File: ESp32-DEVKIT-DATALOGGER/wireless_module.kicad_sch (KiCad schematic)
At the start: 22 parts, among them J201 Socket_01x02, J202 Conn_01x06_Socket, J203 Conn_01x04_Socket, J204 Conn_01x04_Socket, J205 Micro_SD_Card, Q201 MMBT3904, Q202 MMBT3904, SW201 SW_Omron_B3FS, SW202 SW_Omron_B3FS, U201 ESP32-S3-WROOM-1

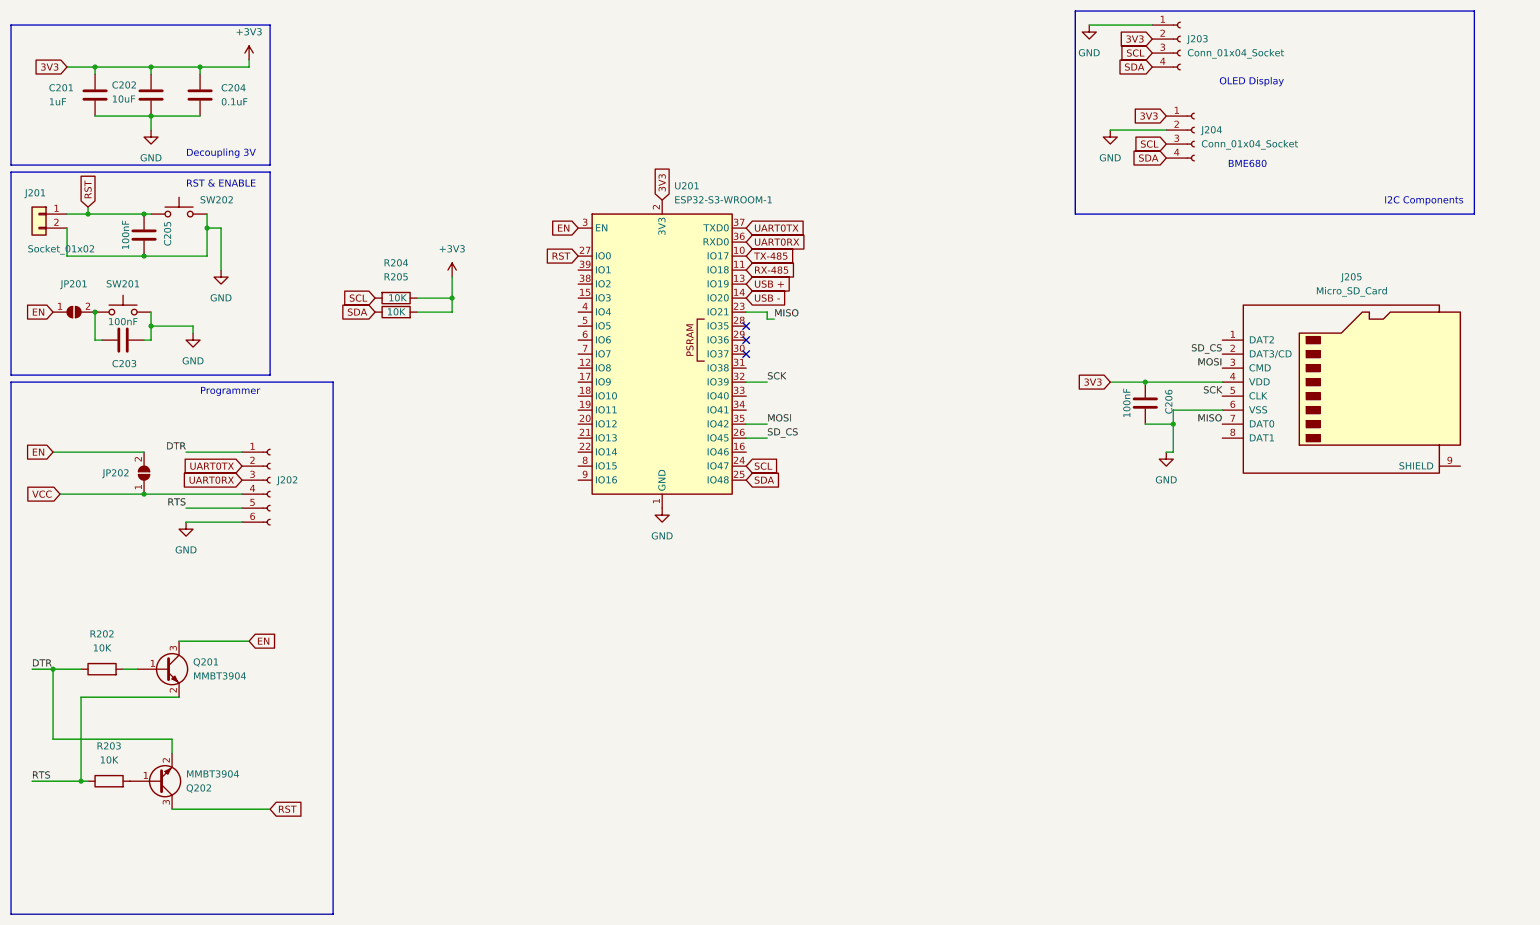
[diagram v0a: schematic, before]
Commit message: Small Changes
Adding I2C components
More RS485
And it is required changing the  Labels for RS485 . for 3 different channels
And Make them ISO Pins
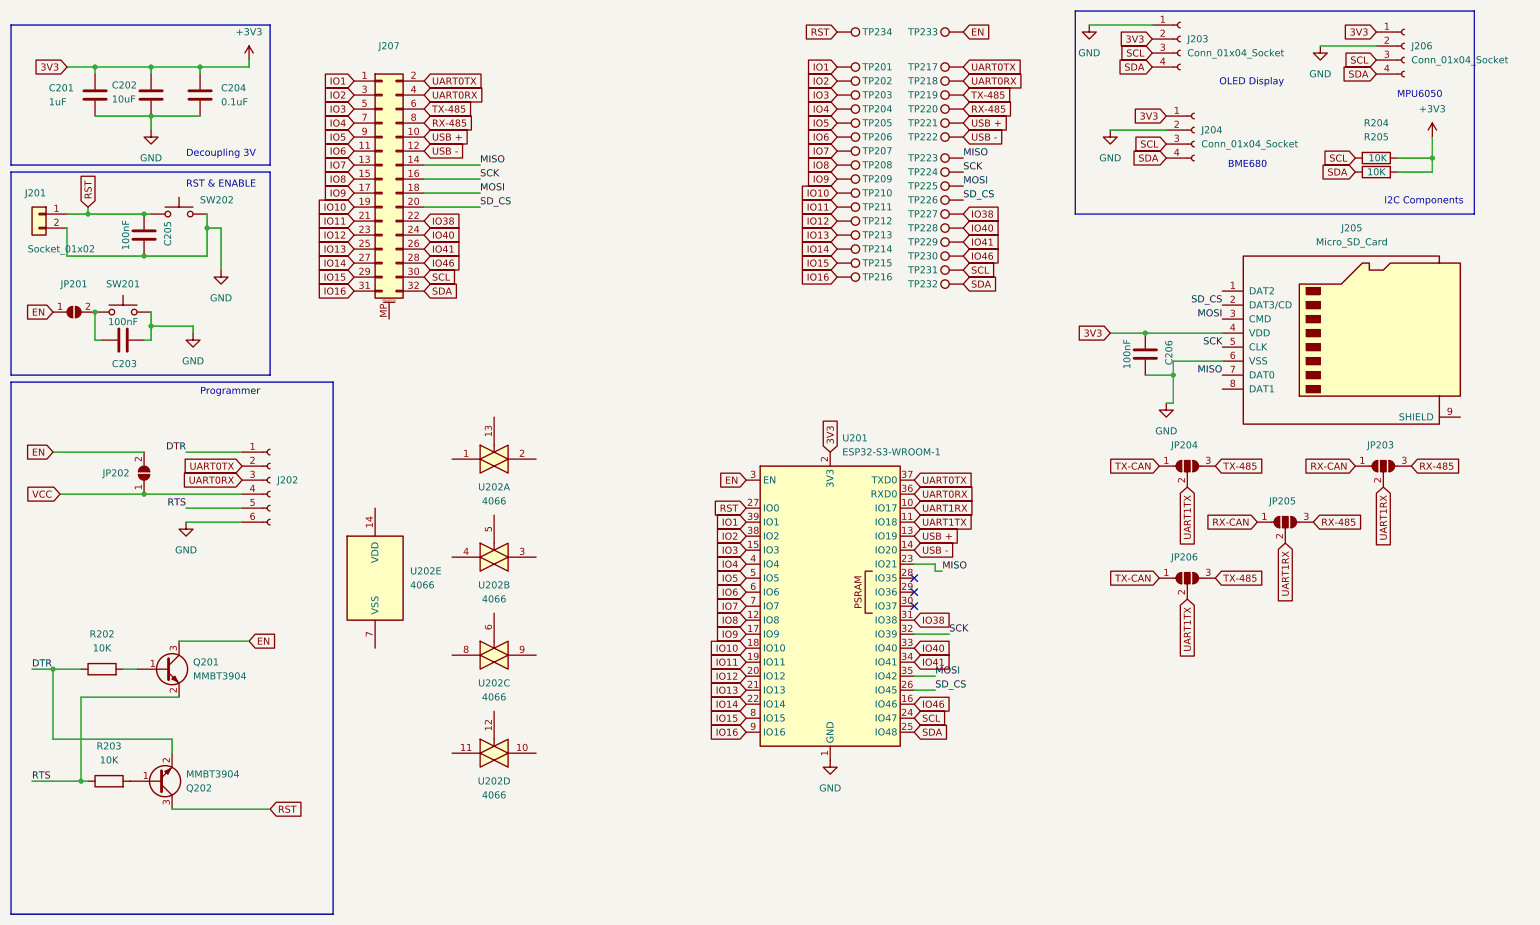
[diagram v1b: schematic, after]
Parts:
- added J206: Conn_01x04_Socket, Connector_PinSocket_2.54mm:PinSocket_1x04_P2.54mm_Vertical, symbol Connector:Conn_01x04_Socket
- added J207: Conn_02x16_Odd_Even_MountingPin, symbol Connector_Generic_MountingPin:Conn_02x16_Odd_Even_MountingPin
- added JP203, JP204, JP205, JP206: SolderJumper_3_Open, Jumper:SolderJumper-3_P2.0mm_Open_TrianglePad1.0x1.5mm, symbol Jumper:SolderJumper_3_Open
- added TP201, TP202, TP203, TP204, TP205, TP206, TP207, TP208, TP209, TP210, TP211, TP212, TP213, TP214, TP215, TP216, TP217, TP218, TP219, TP220, TP221, TP222, TP223, TP224, TP225, TP226, TP227, TP228, TP229, TP230, TP231, TP232, TP233, TP234: TestPoint, TestPoint:TestPoint_Pad_D2.0mm, symbol Connector:TestPoint
- added U202: 4066, symbol 4xxx:4066
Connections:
- net +3V3: now also J206.1 (Pin_1)
- net EN: now also TP233.1
- net GND: now also J206.2 (Pin_2)
- net MISO: now also J207.14 (Pin_14), TP223.1
- net MOSI: now also J207.18 (Pin_18), TP225.1
- net RST: now also TP234.1
- net RX-485: now also J207.8 (Pin_8), JP203.3 (B), JP205.3 (B), TP220.1; no longer U201.11 (IO18)
- net SCK: now also J207.16 (Pin_16), TP224.1
- net SCL: now also J206.3 (Pin_3), J207.30 (Pin_30), TP231.1
- net SDA: now also J206.4 (Pin_4), J207.32 (Pin_32), TP232.1
- net SD_CS: now also J207.20 (Pin_20), TP226.1
- net TX-485: now also J207.6 (Pin_6), JP204.3 (B), JP206.3 (B), TP219.1; no longer U201.10 (IO17)
- net UART0RX: now also J207.4 (Pin_4), TP218.1
- net UART0TX: now also J207.2 (Pin_2), TP217.1
- net USB +: now also J207.10 (Pin_10), TP221.1
- net USB -: now also J207.12 (Pin_12), TP222.1
- net IO8: now reaches U201.12 (IO8)
- net IO8: now also J207.15 (Pin_15), TP208.1
- net IO3: now reaches U201.15 (IO3)
- net IO3: now also J207.5 (Pin_5), TP203.1
- net IO46: now reaches U201.16 (IO46)
- net IO46: now also J207.28 (Pin_28), TP230.1
- net IO9: now reaches U201.17 (IO9)
- net IO9: now also J207.17 (Pin_17), TP209.1
- net IO10: now reaches U201.18 (IO10)
- net IO10: now also J207.19 (Pin_19), TP210.1
- net IO11: now reaches U201.19 (IO11)
- net IO11: now also J207.21 (Pin_21), TP211.1
- net IO12: now reaches U201.20 (IO12)
- net IO12: now also J207.23 (Pin_23), TP212.1
- net IO13: now reaches U201.21 (IO13)
- net IO13: now also J207.25 (Pin_25), TP213.1
- net IO14: now reaches U201.22 (IO14)
- net IO14: now also J207.27 (Pin_27), TP214.1
- net IO38: now reaches U201.31 (IO38)
- net IO38: now also J207.22 (Pin_22), TP227.1
- net IO40: now reaches U201.33 (IO40)
- net IO40: now also J207.24 (Pin_24), TP228.1
- net IO41: now reaches U201.34 (IO41)
- net IO41: now also J207.26 (Pin_26), TP229.1
- net IO2: now reaches U201.38 (IO2)
- net IO2: now also J207.3 (Pin_3), TP202.1
- net IO1: now reaches U201.39 (IO1)
- net IO1: now also J207.1 (Pin_1), TP201.1
- net IO4: now reaches U201.4 (IO4)
- net IO4: now also J207.7 (Pin_7), TP204.1
- net IO5: now reaches U201.5 (IO5)
- net IO5: now also J207.9 (Pin_9), TP205.1
- net IO6: now reaches U201.6 (IO6)
- net IO6: now also J207.11 (Pin_11), TP206.1
- net IO7: now reaches U201.7 (IO7)
- net IO7: now also J207.13 (Pin_13), TP207.1
- net IO15: now reaches U201.8 (IO15)
- net IO15: now also J207.29 (Pin_29), TP215.1
- net IO16: now reaches U201.9 (IO16)
- net IO16: now also J207.31 (Pin_31), TP216.1
- new net RX-CAN: JP203.1 (A), JP205.1 (A)
- new net TX-CAN: JP204.1 (A), JP206.1 (A)
- new net UART1RX: JP203.2 (C), JP205.2 (C), U201.10 (IO17)
- new net UART1TX: JP204.2 (C), JP206.2 (C), U201.11 (IO18)
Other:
- note added: "MPU6050"
- moved on the sheet: C206, J205, R204, R205, U201
